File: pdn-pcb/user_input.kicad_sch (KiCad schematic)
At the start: 20 parts, among them Q1 BJT 2222A, SW1 Primary Button, SW2 Secondary Button

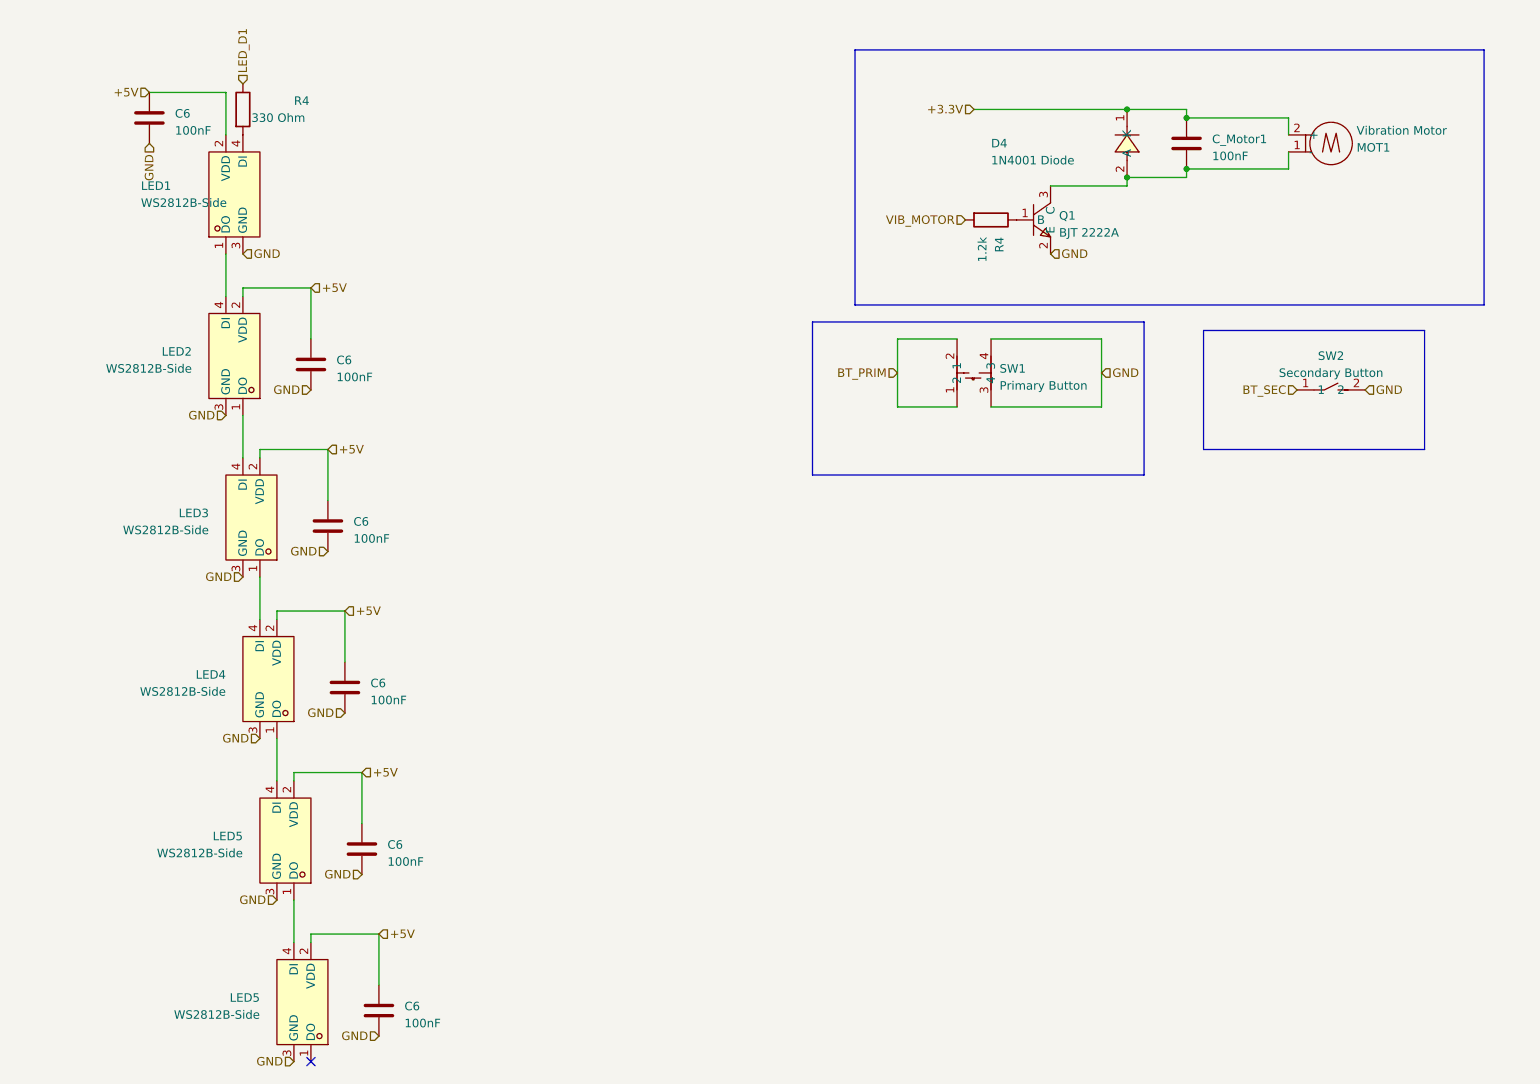
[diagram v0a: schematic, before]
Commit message: Updated 3v3 LDO to an LDL1117, reworked the brain board and added TVS protection.
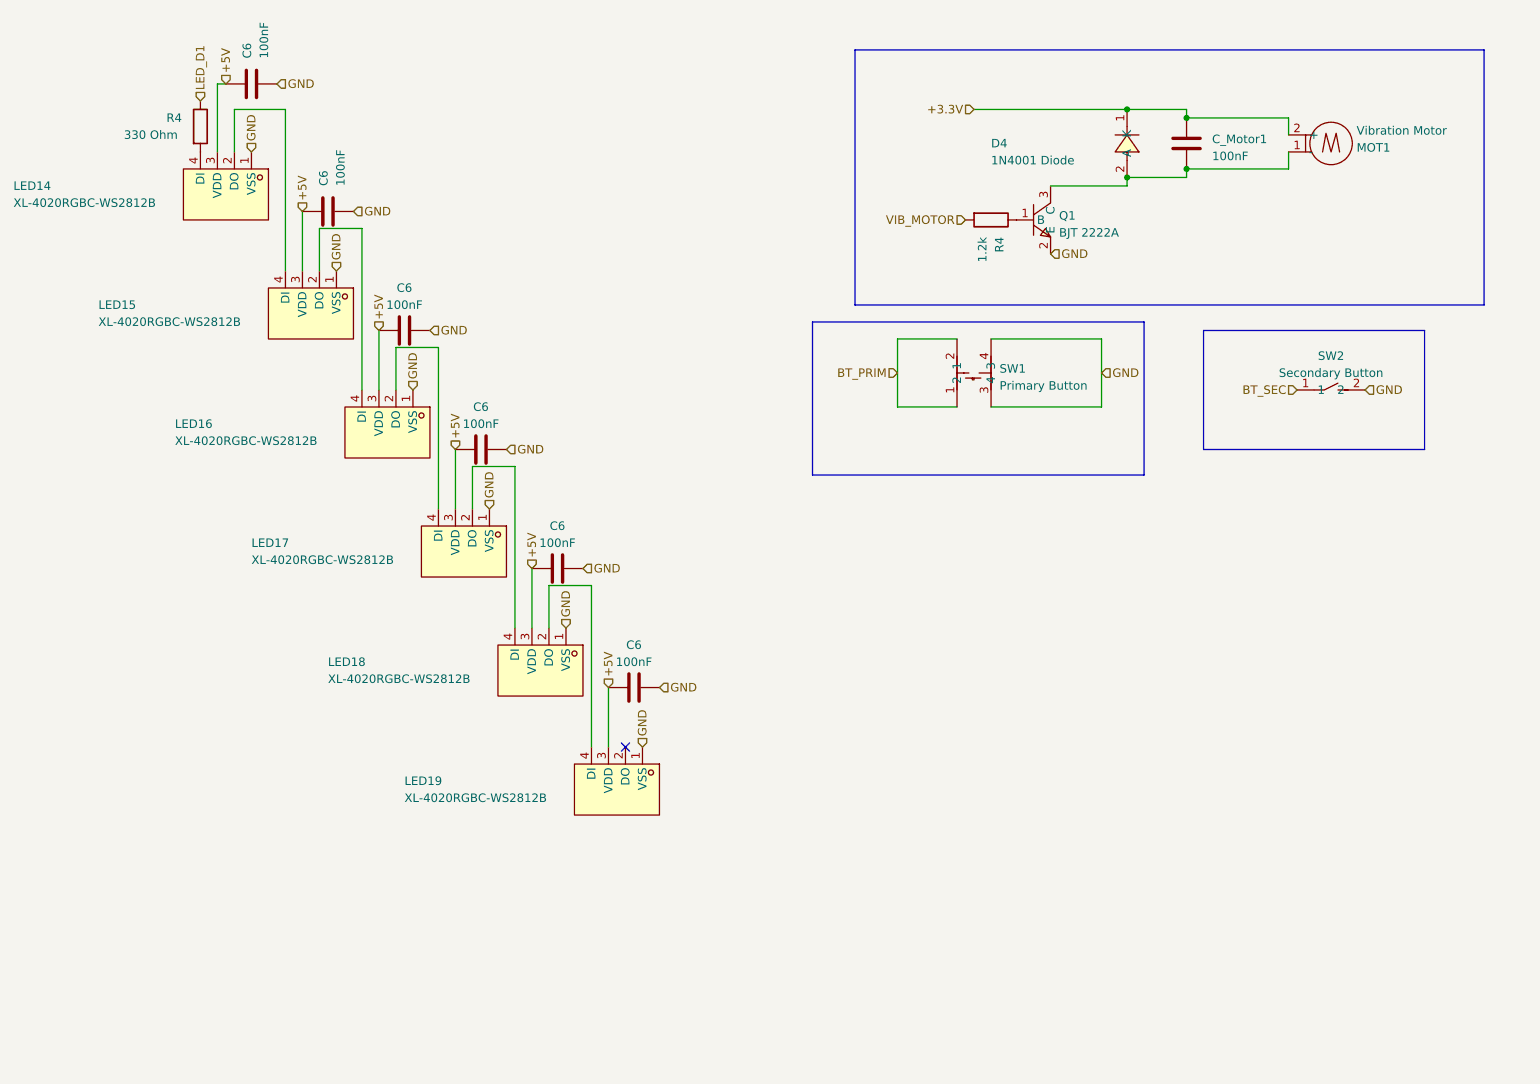
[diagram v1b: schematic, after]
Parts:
- removed LED1, LED2, LED3, LED4, LED5 (x2): WS2812B-Side, global:LED-SMD_4P-L4.0-W1.7_XL-4020RGBC-WS2812B, symbol global:XL-1615RGBC-WS2812B
- added LED14, LED15, LED16, LED17, LED18, LED19: XL-4020RGBC-WS2812B, global:LED-SMD_4P-L4.0-W1.7_XL-4020RGBC-WS2812B, symbol global:XL-4020RGBC-WS2812B
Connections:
- net +5V: now also LED14.3 (VDD), LED15.3 (VDD), LED16.3 (VDD), LED17.3 (VDD), LED18.3 (VDD), LED19.3 (VDD)
- net GND: now also LED14.1 (VSS), LED15.1 (VSS), LED16.1 (VSS), LED17.1 (VSS), LED18.1 (VSS), LED19.1 (VSS)
- net at R4.2: now also LED14.4 (DI)
- new net: LED17.2 (DO), LED18.4 (DI)
- new net: LED16.2 (DO), LED17.4 (DI)
- new net: LED15.2 (DO), LED16.4 (DI)
- new net: LED14.2 (DO), LED15.4 (DI)
- new net: LED18.2 (DO), LED19.4 (DI)
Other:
- moved on the sheet: C6, R4

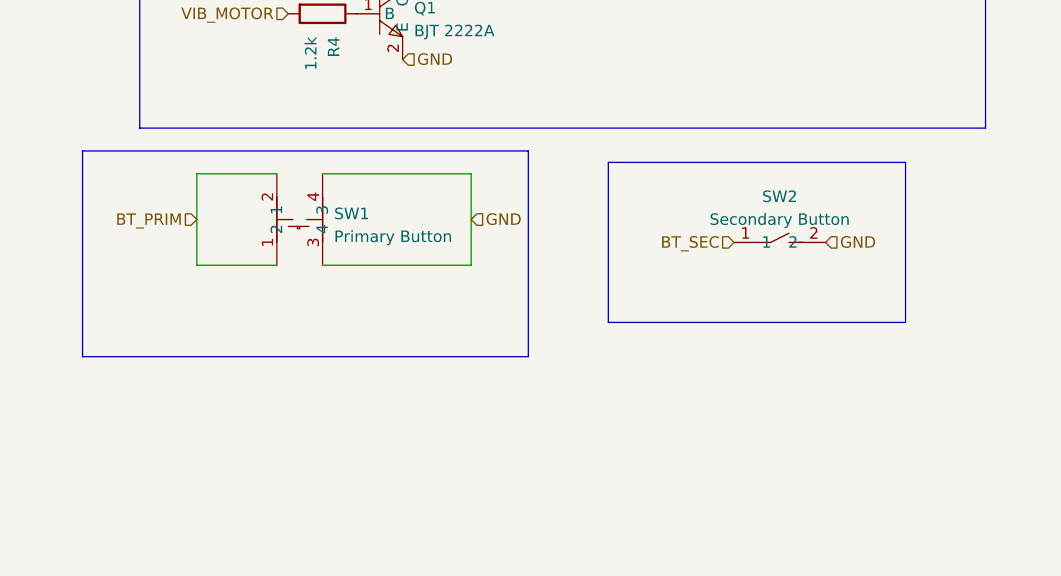
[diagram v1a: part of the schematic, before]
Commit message: Updated display, user board and display board.
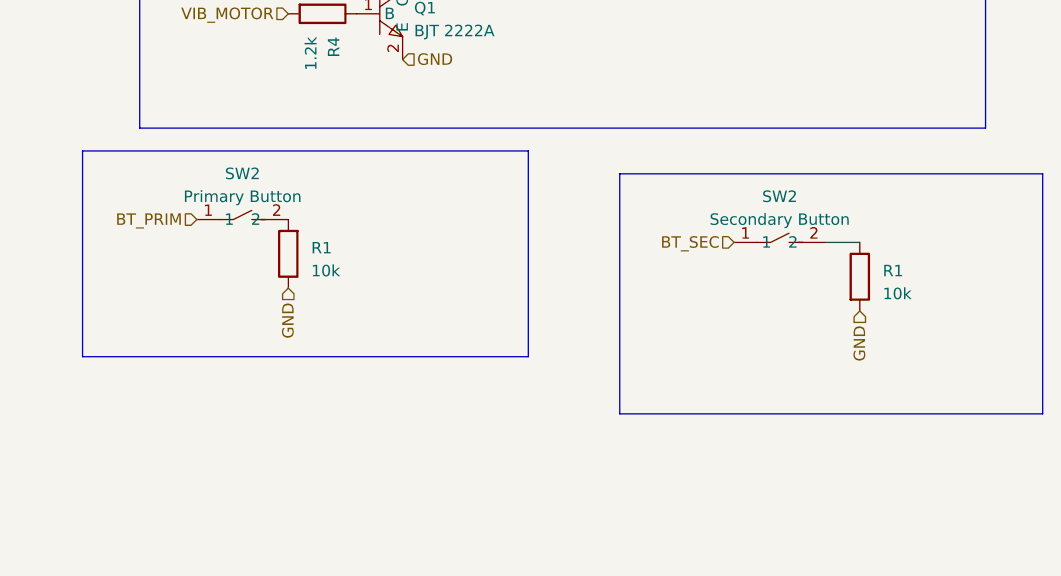
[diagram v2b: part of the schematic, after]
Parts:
- removed SW1: Primary Button, global:KEY-SMD_4P-L4.2-W3.2-P2.20-LS4.6, symbol global:SKRPASE010
- added R1 (x2): 10k, Resistor_SMD:R_0603_1608Metric, symbol Device:R
- added SW2: Primary Button, global:KEY-SMD_L6.0-W3.5-LS8.0, symbol global:TSB013A5026B
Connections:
- net BT_PRIM: now also SW2.1
- net GND: now also R1.1, R1.2; no longer SW2.2
- new net: R1.2, SW2.2
- new net: R1.1, SW2.2
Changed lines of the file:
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@@
-    (stroke (width 0) (type default))
-  )
-  (wire (pts (xy 135.89 102.87) (xy 127 102.87))
     (stroke (width 0) (type default))
   )
@@
     (stroke (width 0) (type default))
   )
-  (wire (pts (xy 157.48 92.71) (xy 157.48 102.87))
-    (stroke (width 0) (type default))
-  )
-  (wire (pts (xy 157.48 102.87) (xy 140.97 102.87))
-    (stroke (width 0) (type default))
-  )
   (wire (pts (xy 81.28 129.54) (xy 81.28 153.67))
     (stroke (width 0) (type default))
   )
-  (wire (pts (xy 127 92.71) (xy 127 102.87))
-    (stroke (width 0) (type default))
-  )
   (wire (pts (xy 58.42 93.98) (xy 58.42 118.11))
     (stroke (width 0) (type default))
@@
     (stroke (width 0) (type default))
   )
-  (wire (pts (xy 140.97 92.71) (xy 157.48 92.71))
-    (stroke (width 0) (type default))
-  )
   (wire (pts (xy 161.29 68.58) (xy 170.18 68.58))
     (stroke (width 0) (type default))
@@
     (stroke (width 0) (type default))
   )
-  (wire (pts (xy 127 92.71) (xy 135.89 92.71))
+  (wire (pts (xy 200.66 100.33) (xy 196.85 100.33))
     (stroke (width 0) (type default))
   )
@@
     (fill (type none))
   )
-  (rectangle (start 172.72 91.44) (end 205.74 109.22)
+  (rectangle (start 173.99 92.71) (end 220.98 119.38)
     (stroke (width 0) (type default))
     (fill (type none))
@@
       (effects (font (size 1.27 1.27)) (justify left) hide)
     )
-  )
-  (hierarchical_label "GND" (shape input) (at 157.48 97.79 0) (fields_autoplaced)
-    (effects (font (size 1.27 1.27)) (justify left))
   )
   (hierarchical_label "GND" (shape input) (at 68.58 109.22 0) (fields_autoplaced)
@@
     )
   )
-  (hierarchical_label "GND" (shape input) (at 196.85 100.33 0) (fields_autoplaced)
-    (effects (font (size 1.27 1.27)) (justify left))
-  )
   (hierarchical_label "+5V" (shape input) (at 60.96 109.22 90) (fields_autoplaced)
     (effects (font (size 1.27 1.27)) (justify left))
@@
     )
   )
+  (hierarchical_label "GND" (shape input) (at 200.66 107.95 270) (fields_autoplaced)
+    (effects (font (size 1.27 1.27)) (justify right))
+  )
+  (hierarchical_label "GND" (shape input) (at 137.16 105.41 270) (fields_autoplaced)
+    (effects (font (size 1.27 1.27)) (justify right))
+  )
   (hierarchical_label "GND" (shape input) (at 45.72 73.66 0) (fields_autoplaced)
     (effects (font (size 1.27 1.27)) (justify left))
@@
     )
   )
+  (symbol (lib_id "Device:R") (at 137.16 101.6 180) (unit 1)
+    (in_bom yes) (on_board yes) (dnp no) (fields_autoplaced)
+    (property "Reference" "R1" (at 139.7 100.965 0)
+      (effects (font (size 1.27 1.27)) (justify right))
+    )
+    (property "Value" "10k" (at 139.7 103.505 0)
+      (effects (font (size 1.27 1.27)) (justify right))
+    )
+    (property "Footprint" "Resistor_SMD:R_0603_1608Metric" (at 138.938 101.6 90)
+      (effects (font (size 1.27 1.27)) hide)
+    )
+    (property "Datasheet" "~" (at 137.16 101.6 0)
+      (effects (font (size 1.27 1.27)) hide)
+    )
+    (property "LCSC Part" "C103199" (at 137.16 101.6 0)
+      (effects (font (size 1.27 1.27)) hide)
+    )
+    (pin "1")
+    (pin "2")
+    (instances
+      (project "hex_lights"
+        (path "/99dd32be-e52f-4355-ae8e-2bf6a0d7d0ad"
+          (reference "R1") (unit 1)
+        )
+      )
+      (project "PDN"
+        (path "/df0bc267-025e-4c4e-a09b-51ff87d0c1db"
+          (reference "R_EN1") (unit 1)
+        )
+        (path "/df0bc267-025e-4c4e-a09b-51ff87d0c1db/5528999e-e72f-4e39-b507-18d3b44f3b41"
+          (reference "R12") (unit 1)
+        )
+        (path "/df0bc267-025e-4c4e-a09b-51ff87d0c1db/176b62b0-12ec-4a4a-9309-4e23e06b21ff"
+          (reference "R16") (unit 1)
+        )
+      )
+      (project "PDN"
+        (path "/ef110d8b-8fcf-4e68-8407-a270a2f7664a"
+          (reference "R1") (unit 1)
+        )
+      )
+    )
+  )
   (symbol (lib_id "Device:C") (at 64.77 109.22 90) (unit 1)
     (in_bom yes) (on_board yes) (dnp no) (fields_autoplaced)
@@
         (path "/ef110d8b-8fcf-4e68-8407-a270a2f7664a"
           (reference "C5") (unit 1)
+        )
+      )
+    )
+  )
+  (symbol (lib_id "Device:R") (at 200.66 104.14 0) (unit 1)
+    (in_bom yes) (on_board yes) (dnp no) (fields_autoplaced)
+    (property "Reference" "R1" (at 203.2 103.505 0)
+      (effects (font (size 1.27 1.27)) (justify left))
+    )
+    (property "Value" "10k" (at 203.2 106.045 0)
+      (effects (font (size 1.27 1.27)) (justify left))
+    )
+    (property "Footprint" "Resistor_SMD:R_0603_1608Metric" (at 198.882 104.14 90)
+      (effects (font (size 1.27 1.27)) hide)
+    )
+    (property "Datasheet" "~" (at 200.66 104.14 0)
+      (effects (font (size 1.27 1.27)) hide)
+    )
+    (property "LCSC Part" "C103199" (at 200.66 104.14 0)
+      (effects (font (size 1.27 1.27)) hide)
+    )
+    (pin "1")
+    (pin "2")
+    (instances
+      (project "hex_lights"
+        (path "/99dd32be-e52f-4355-ae8e-2bf6a0d7d0ad"
+          (reference "R1") (unit 1)
+        )
+      )
+      (project "PDN"
+        (path "/df0bc267-025e-4c4e-a09b-51ff87d0c1db"
+          (reference "R_EN1") (unit 1)
+        )
+        (path "/df0bc267-025e-4c4e-a09b-51ff87d0c1db/5528999e-e72f-4e39-b507-18d3b44f3b41"
+          (reference "R12") (unit 1)
+        )
+        (path "/df0bc267-025e-4c4e-a09b-51ff87d0c1db/176b62b0-12ec-4a4a-9309-4e23e06b21ff"
+          (reference "R17") (unit 1)
+        )
+      )
+      (project "PDN"
+        (path "/ef110d8b-8fcf-4e68-8407-a270a2f7664a"
+          (reference "R1") (unit 1)
         )
       )
@@
     )
   )
-  (symbol (lib_id "global:SKRPASE010") (at 138.43 97.79 90) (unit 1)
-    (in_bom yes) (on_board yes) (dnp no) (fields_autoplaced)
-    (property "Reference" "SW1" (at 142.24 97.155 90)
-      (effects (font (size 1.27 1.27)) (justify right))
-    )
-    (property "Value" "Primary Button" (at 142.24 99.695 90)
-      (effects (font (size 1.27 1.27)) (justify right))
-    )
-    (property "Footprint" "global:KEY-SMD_4P-L4.2-W3.2-P2.20-LS4.6" (at 148.59 97.79 0)
-      (effects (font (size 1.27 1.27)) hide)
-    )
-    (property "Datasheet" "https://lcsc.com/product-detail/Tactile-Switches_ALPS-Electric-SKRPASE010_C470427.html" (at 151.13 97.79 0)
-      (effects (font (size 1.27 1.27)) hide)
-    )
-    (property "LCSC Part" "C470427" (at 153.67 97.79 0)
-      (effects (font (size 1.27 1.27)) hide)
-    )
-    (pin "1")
-    (pin "2")
-    (pin "3")
-    (pin "4")
-    (instances
-      (project "PDN"
-        (path "/df0bc267-025e-4c4e-a09b-51ff87d0c1db"
-          (reference "SW1") (unit 1)
-        )
-        (path "/df0bc267-025e-4c4e-a09b-51ff87d0c1db/176b62b0-12ec-4a4a-9309-4e23e06b21ff"
-          (reference "SW2") (unit 1)
-        )
-      )
-    )
-  )
   (symbol (lib_id "Device:C") (at 87.63 144.78 90) (unit 1)
     (in_bom yes) (on_board yes) (dnp no) (fields_autoplaced)
@@
         )
       )
+    )
+  )
+  (symbol (lib_id "global:TSB013A5026B") (at 132.08 97.79 0) (unit 1)
+    (in_bom yes) (on_board yes) (dnp no) (fields_autoplaced)
+    (property "Reference" "SW2" (at 132.08 92.71 0)
+      (effects (font (size 1.27 1.27)))
+    )
+    (property "Value" "Primary Button" (at 132.08 95.25 0)
+      (effects (font (size 1.27 1.27)))
+    )
+    (property "Footprint" "global:KEY-SMD_L6.0-W3.5-LS8.0" (at 132.08 105.41 0)
+      (effects (font (size 1.27 1.27)) hide)
+    )
+    (property "Datasheet" "" (at 132.08 97.79 0)
+      (effects (font (size 1.27 1.27)) hide)
+    )
+    (property "LCSC Part" "C2888463" (at 132.08 107.95 0)
+      (effects (font (size 1.27 1.27)) hide)
+    )
+    (pin "1")
+    (pin "2")
+    (instances
+      (project "PDN"
+        (path "/df0bc267-025e-4c4e-a09b-51ff87d0c1db"
+          (reference "SW2") (unit 1)
+        )
+        (path "/df0bc267-025e-4c4e-a09b-51ff87d0c1db/176b62b0-12ec-4a4a-9309-4e23e06b21ff"
+          (reference "SW2") (unit 1)
+        )
+      )
